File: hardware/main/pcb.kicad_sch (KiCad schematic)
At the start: 22 parts, among them J1 Conn_01x02_Socket, J2 Conn_01x02_Socket

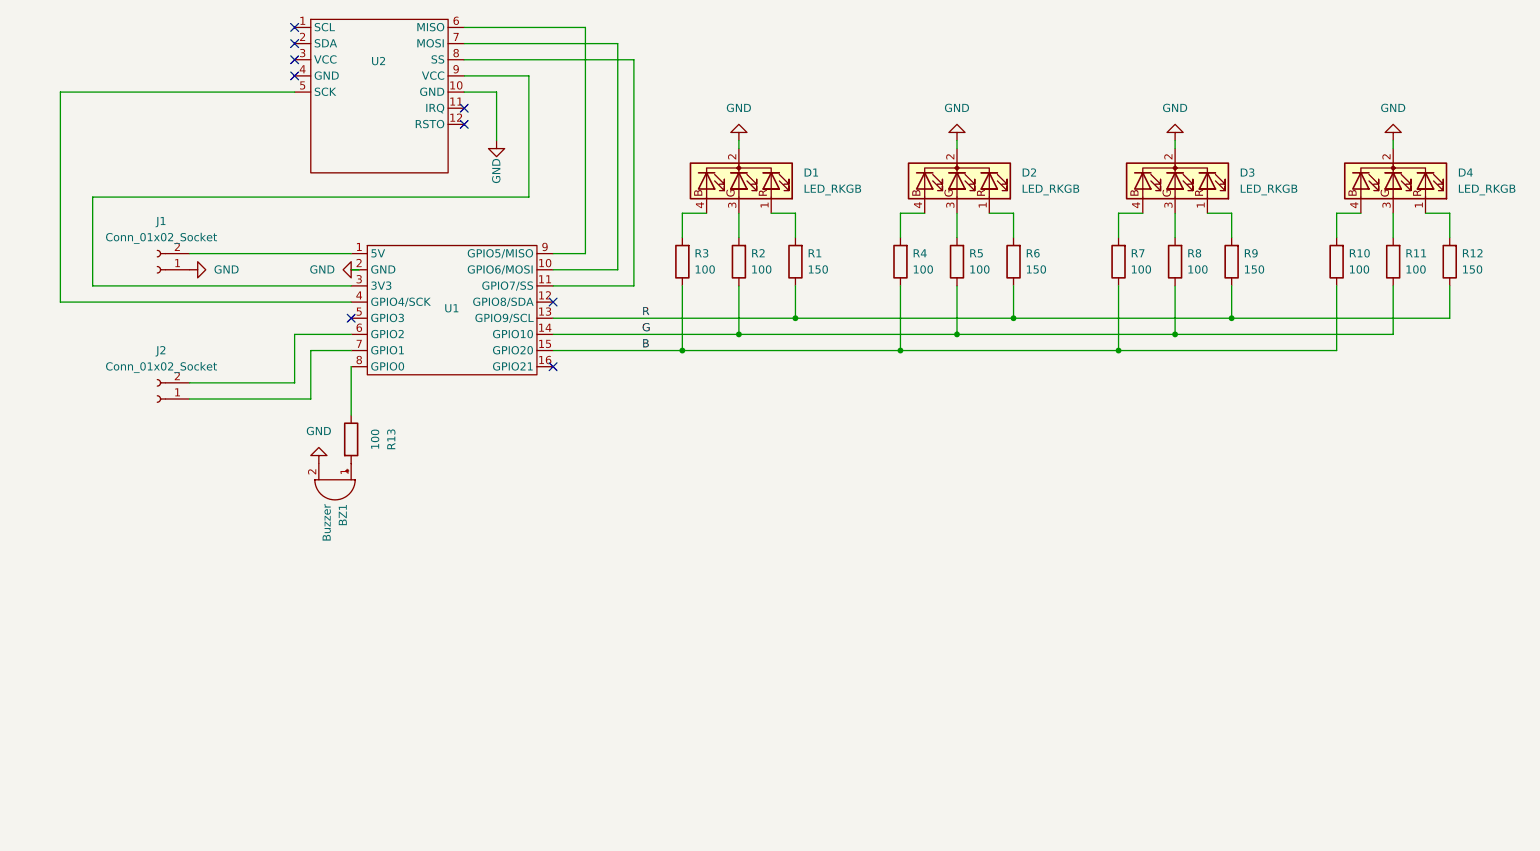
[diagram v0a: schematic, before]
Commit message: Add transistor to led line (#18)
* add trasistors to for led diode board

* update the pcb design

* update the board

* update config pin out

* add github action to render PCB before/after on PRs

Adds a KiBot-based workflow that renders the bottom side of the main PCB
at the PR base SHA and at the head SHA, pushes both PNGs to a dedicated
pcb-pr-previews orphan branch, and posts/updates a single PR comment
with the two images side-by-side so reviewers can see what changed
without checking out the branch.

Co-Authored-By: Claude Opus 4.7 (1M context) <noreply@anthropic.com>

* add gerber file

* add 3mf file for box

* turn on end to end for pr1

* add led pcb

---------

Co-authored-by: Claude Opus 4.7 (1M context) <noreply@anthropic.com>
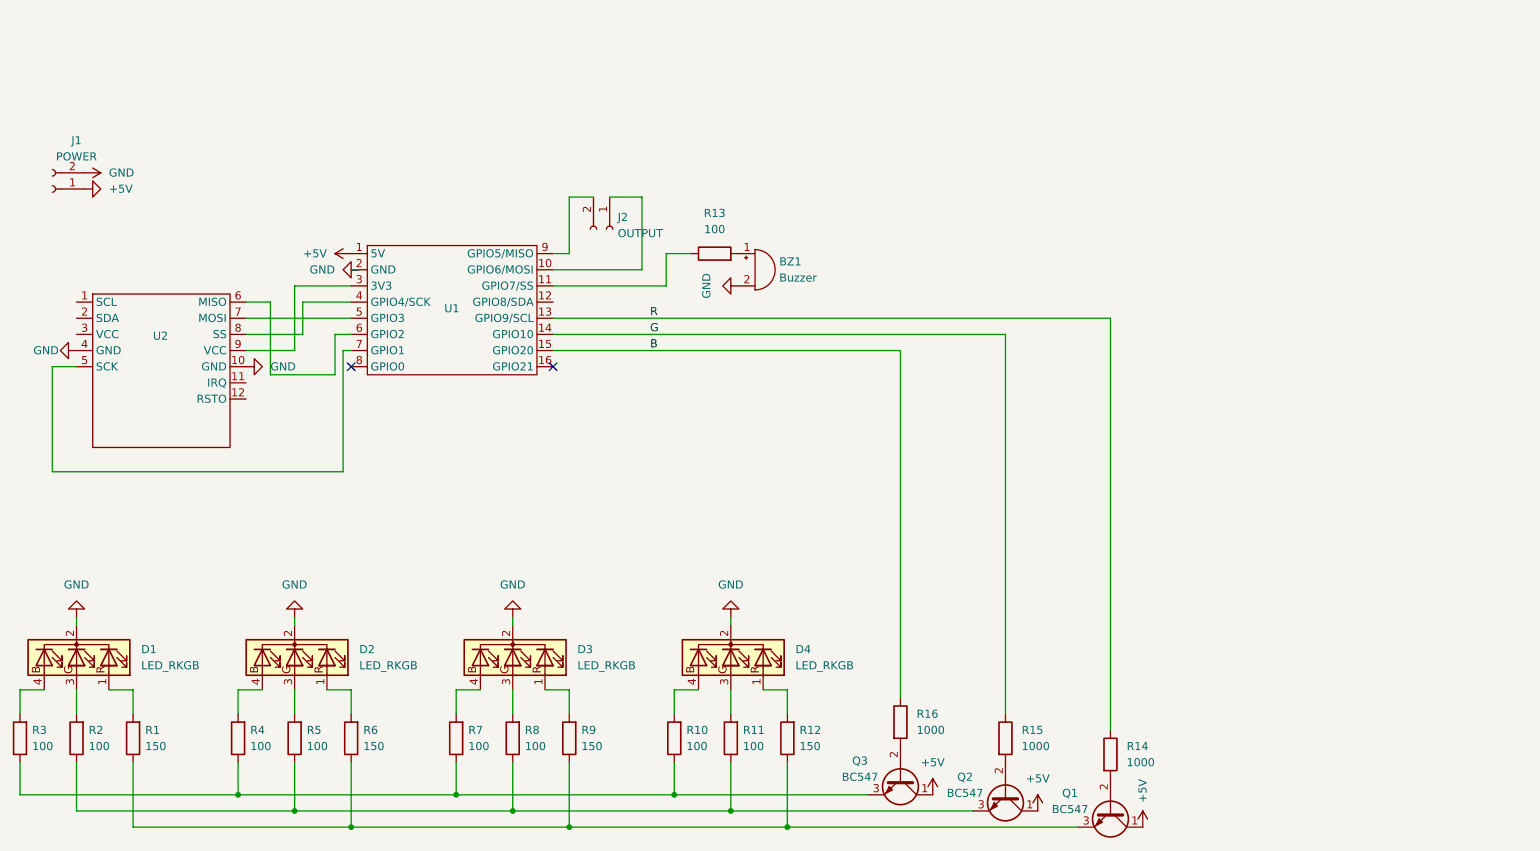
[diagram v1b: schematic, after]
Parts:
- added Q1, Q2, Q3: BC547, Package_TO_SOT_THT:TO-92_Inline, symbol Transistor_BJT:BC547
- added R14, R15, R16: 1000, Resistor_THT:CNC_Ready_R_Axial_DIN0204_L3.6mm_D1.6mm_P7.62mm_Horizontal, symbol Device:R
- J1: value Conn_01x02_Socket -> POWER; footprint TerminalBlock_Phoenix:TerminalBlock_Phoenix_MKDS-1,5-2-5.08_1x02_P5.08mm_Horizontal -> Connector_Molex:Molex_Nano-Fit_105313-xx02_1x02_P2.50mm_Horizontal
- J2: value Conn_01x02_Socket -> OUTPUT; footprint TerminalBlock_Phoenix:TerminalBlock_Phoenix_MKDS-1,5-2-5.08_1x02_P5.08mm_Horizontal -> Connector_Molex:Molex_Nano-Fit_105313-xx02_1x02_P2.50mm_Horizontal
- U1: footprint esp_32_c3_supper_mini:esp_32_c3_supper_mini_tht_smd -> esp_32_c3_supper_mini:esp_32_c3_supper_mini
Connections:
- net B: now also R16.1; no longer R10.1, R3.1, R4.1, R7.1
- net G: now also R15.1; no longer R11.1, R2.1, R5.1, R8.1
- net GND: now also J1.2 (Pin_2), U2.4 (GND); no longer J1.1 (Pin_1)
- net R: now also R14.1; no longer R1.1, R12.1, R6.1, R9.1
- net at U2.5 (SCK): now also U1.7 (GPIO1); no longer U1.4 (GPIO4/SCK)
- net at U2.6 (MISO): now also U1.6 (GPIO2); no longer U1.9 (GPIO5/MISO)
- net at U2.7 (MOSI): now also U1.5 (GPIO3); no longer U1.10 (GPIO6/MOSI)
- net at U2.8 (SS): now also U1.4 (GPIO4/SCK); no longer U1.11 (GPIO7/SS)
- net at R13.1: now also U1.11 (GPIO7/SS); no longer U1.8 (GPIO0)
- net +5V: now reaches U1.1 (5V)
- net +5V: now also J1.1 (Pin_1), Q1.1 (C), Q2.1 (C), Q3.1 (C); no longer J1.2 (Pin_2)
- net at J2.2 (Pin_2): now also U1.9 (GPIO5/MISO); no longer U1.6 (GPIO2)
- net at J2.1 (Pin_1): now also U1.10 (GPIO6/MOSI); no longer U1.7 (GPIO1)
- new net: Q3.3 (E), R10.1, R3.1, R4.1, R7.1
- new net: Q1.3 (E), R1.1, R12.1, R6.1, R9.1
- new net: Q2.3 (E), R11.1, R2.1, R5.1, R8.1
- new net: Q3.2 (B), R16.2
- new net: Q2.2 (B), R15.2
- new net: Q1.2 (B), R14.2
- no-connect marks 9 -> 2
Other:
- moved on the sheet: BZ1, D1, D2, D3, D4, J1, J2, R1, R10, R11, R12, R13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
